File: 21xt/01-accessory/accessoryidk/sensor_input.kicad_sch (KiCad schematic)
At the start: 22 parts, among them IC5 INA821IDGKT, IC6 TXB0108PWR, IC8 INA821IDGKT, IC9 INA821IDGKT, J2 5747847-6, J3 Conn_01x11, J4 Conn_01x11, J5 Conn_01x11

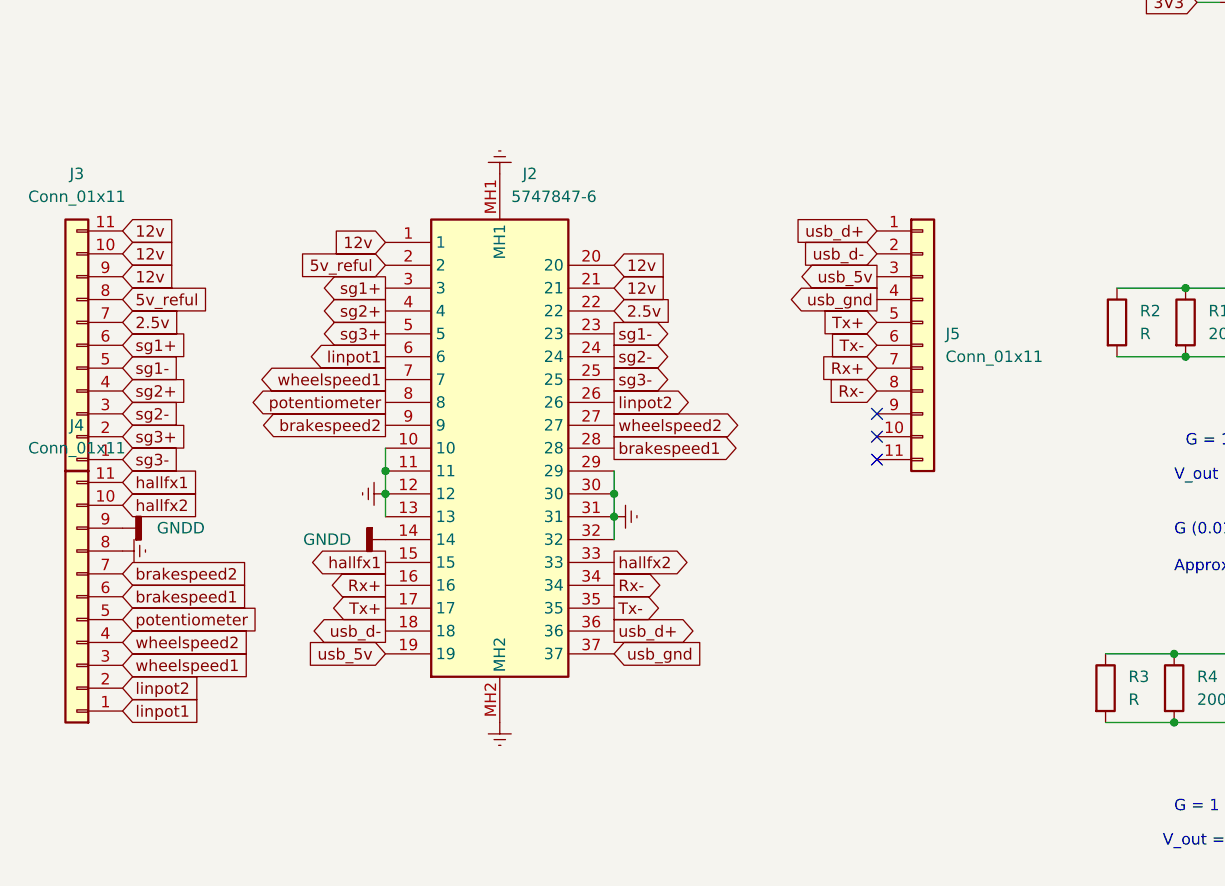
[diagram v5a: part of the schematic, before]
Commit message: Revising accessory schematic
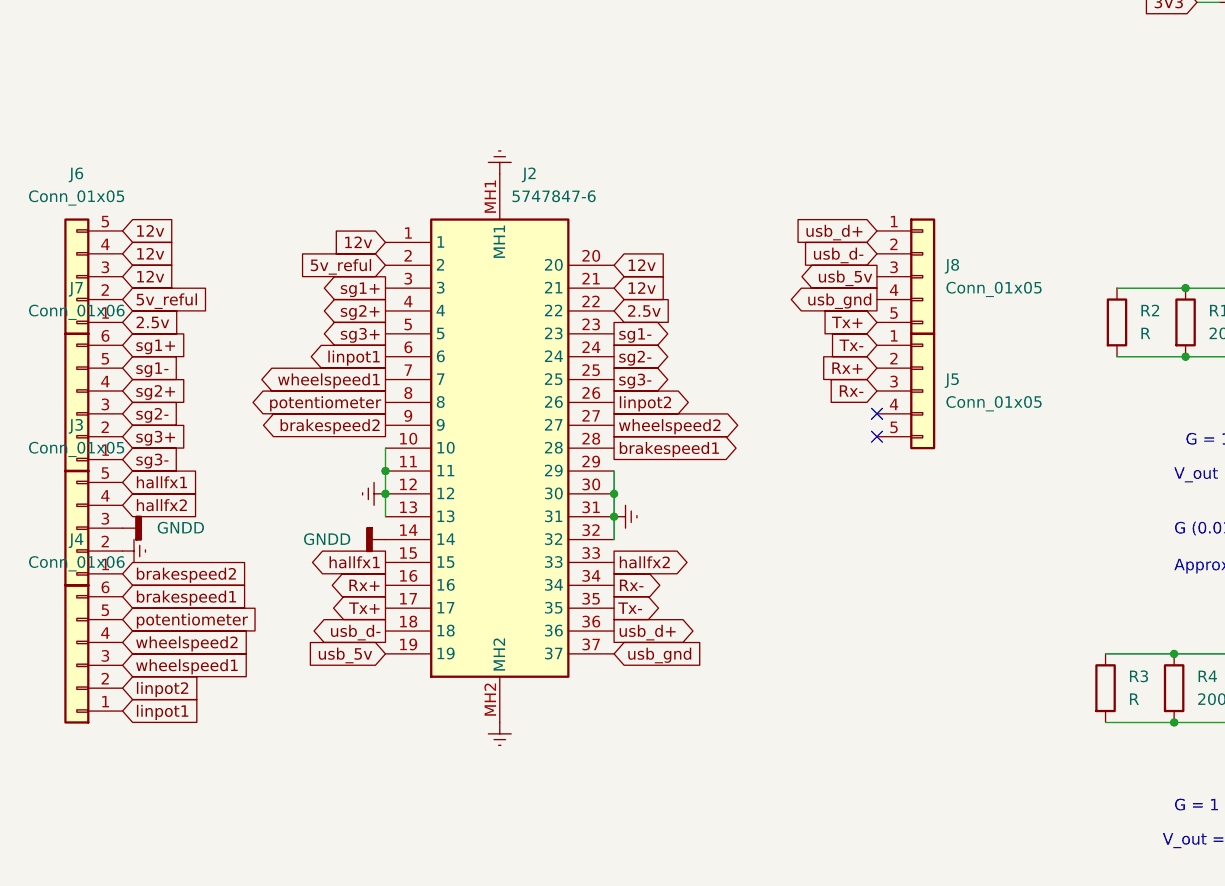
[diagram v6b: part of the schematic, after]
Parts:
- removed J3, J4, J5: Conn_01x11, Connector_JST:JST_EH_B11B-EH-A_1x11_P2.50mm_Vertical, symbol Connector_Generic:Conn_01x11
- added J3, J5, J6, J8: Conn_01x05, symbol Connector_Generic:Conn_01x05
- added J4, J7: Conn_01x06, symbol Connector_Generic:Conn_01x06
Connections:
- net 12v: now also J6.3 (Pin_3), J6.4 (Pin_4), J6.5 (Pin_5)
- net 2.5v: now also J6.1 (Pin_1)
- net 5v_buck: now also J8.3 (Pin_3)
- net 5v_reful: now also J6.2 (Pin_2)
- net Earth: now also J3.2 (Pin_2)
- net GND: now also J8.4 (Pin_4)
- net GNDD: now also J3.3 (Pin_3)
- net Rx+: now also J5.2 (Pin_2)
- net Rx-: now also J5.3 (Pin_3)
- net Tx+: now also J8.5 (Pin_5)
- net Tx-: now also J5.1 (Pin_1)
- net brakespeed1: now also J4.6 (Pin_6)
- net brakespeed2: now also J3.1 (Pin_1)
- net hallfx1: now also J3.5 (Pin_5)
- net hallfx2: now also J3.4 (Pin_4)
- net linpot1: now also J4.1 (Pin_1)
- net linpot2: now also J4.2 (Pin_2)
- net potentiometer: now also J4.5 (Pin_5)
- net sg1+: now also J7.6 (Pin_6)
- net sg1-: now also J7.5 (Pin_5)
- net sg2+: now also J7.4 (Pin_4)
- net sg2-: now also J7.3 (Pin_3)
- net sg3+: now also J7.2 (Pin_2)
- net sg3-: now also J7.1 (Pin_1)
- net usb_d+: now also J8.1 (Pin_1)
- net usb_d-: now also J8.2 (Pin_2)
- net wheelspeed1: now also J4.3 (Pin_3)
- net wheelspeed2: now also J4.4 (Pin_4)
- no-connect marks 15 -> 14
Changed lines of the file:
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@@
   )
   (no_connect (at 143.51 43.18))
-  (no_connect (at 105.41 101.6))
   (no_connect (at 171.45 35.56))
   (no_connect (at 171.45 45.72))
@@
     )
   )
-  (symbol (lib_id "Connector_Generic:Conn_01x11") (at 110.49 88.9 0) (unit 1)
-    (in_bom yes) (on_board yes) (dnp no) (fields_autoplaced)
-    (property "Reference" "J5" (at 113.03 87.63 0)
-      (effects (font (size 1.27 1.27)) (justify left))
-    )
-    (property "Value" "Conn_01x11" (at 113.03 90.17 0)
-      (effects (font (size 1.27 1.27)) (justify left))
-    )
-    (property "Footprint" "Connector_JST:JST_EH_B11B-EH-A_1x11_P2.50mm_Vertical" (at 110.49 88.9 0)
-      (effects (font (size 1.27 1.27)) hide)
-    )
-    (property "Datasheet" "~" (at 110.49 88.9 0)
-      (effects (font (size 1.27 1.27)) hide)
-    )
-    (pin "9")
-    (pin "2")
-    (pin "3")
-    (pin "4")
-    (pin "11")
-    (pin "1")
-    (pin "10")
-    (pin "5")
-    (pin "8")
-    (pin "7")
-    (pin "6")
-    (instances
-      (project "accessoryidk"
-        (path "/5dacc41e-ffff-47d3-9300-200c6018c603/67100f97-5262-4274-9380-0583de02d6bc"
-          (reference "J5") (unit 1)
-        )
-      )
-    )
-  )
   (symbol (lib_id "power:GND") (at 191.77 81.28 90) (unit 1)
     (in_bom yes) (on_board yes) (dnp no) (fields_autoplaced)
@@
         (path "/5dacc41e-ffff-47d3-9300-200c6018c603/67100f97-5262-4274-9380-0583de02d6bc"
           (reference "#PWR022") (unit 1)
-        )
-      )
-    )
-  )
-  (symbol (lib_id "Connector_Generic:Conn_01x11") (at 16.51 116.84 180) (unit 1)
-    (in_bom yes) (on_board yes) (dnp no) (fields_autoplaced)
-    (property "Reference" "J4" (at 16.51 97.79 0)
-      (effects (font (size 1.27 1.27)))
-    )
-    (property "Value" "Conn_01x11" (at 16.51 100.33 0)
-      (effects (font (size 1.27 1.27)))
-    )
-    (property "Footprint" "Connector_JST:JST_EH_B11B-EH-A_1x11_P2.50mm_Vertical" (at 16.51 116.84 0)
-      (effects (font (size 1.27 1.27)) hide)
-    )
-    (property "Datasheet" "~" (at 16.51 116.84 0)
-      (effects (font (size 1.27 1.27)) hide)
-    )
-    (pin "9")
-    (pin "2")
-    (pin "3")
-    (pin "4")
-    (pin "11")
-    (pin "1")
-    (pin "10")
-    (pin "5")
-    (pin "8")
-    (pin "7")
-    (pin "6")
-    (instances
-      (project "accessoryidk"
-        (path "/5dacc41e-ffff-47d3-9300-200c6018c603/67100f97-5262-4274-9380-0583de02d6bc"
-          (reference "J4") (unit 1)
-        )
-      )
-    )
-  )
-  (symbol (lib_id "Connector_Generic:Conn_01x11") (at 16.51 88.9 180) (unit 1)
-    (in_bom yes) (on_board yes) (dnp no) (fields_autoplaced)
-    (property "Reference" "J3" (at 16.51 69.85 0)
-      (effects (font (size 1.27 1.27)))
-    )
-    (property "Value" "Conn_01x11" (at 16.51 72.39 0)
-      (effects (font (size 1.27 1.27)))
-    )
-    (property "Footprint" "Connector_JST:JST_EH_B11B-EH-A_1x11_P2.50mm_Vertical" (at 16.51 88.9 0)
-      (effects (font (size 1.27 1.27)) hide)
-    )
-    (property "Datasheet" "~" (at 16.51 88.9 0)
-      (effects (font (size 1.27 1.27)) hide)
-    )
-    (pin "9")
-    (pin "2")
-    (pin "3")
-    (pin "4")
-    (pin "11")
-    (pin "1")
-    (pin "10")
-    (pin "5")
-    (pin "8")
-    (pin "7")
-    (pin "6")
-    (instances
-      (project "accessoryidk"
-        (path "/5dacc41e-ffff-47d3-9300-200c6018c603/67100f97-5262-4274-9380-0583de02d6bc"
-          (reference "J3") (unit 1)
         )
       )
@@
     )
   )
+  (symbol (lib_id "Connector_Generic:Conn_01x05") (at 16.51 109.22 180) (unit 1)
+    (in_bom yes) (on_board yes) (dnp no) (fields_autoplaced)
+    (property "Reference" "J3" (at 16.51 97.79 0)
+      (effects (font (size 1.27 1.27)))
+    )
+    (property "Value" "Conn_01x05" (at 16.51 100.33 0)
+      (effects (font (size 1.27 1.27)))
+    )
+    (property "Footprint" "" (at 16.51 109.22 0)
+      (effects (font (size 1.27 1.27)) hide)
+    )
+    (property "Datasheet" "~" (at 16.51 109.22 0)
+      (effects (font (size 1.27 1.27)) hide)
+    )
+    (pin "5")
+    (pin "4")
+    (pin "3")
+    (pin "2")
+    (pin "1")
+    (instances
+      (project "accessoryidk"
+        (path "/5dacc41e-ffff-47d3-9300-200c6018c603/67100f97-5262-4274-9380-0583de02d6bc"
+          (reference "J3") (unit 1)
+        )
+      )
+    )
+  )
   (symbol (lib_id "power:GND") (at 267.97 121.92 90) (unit 1)
     (in_bom yes) (on_board yes) (dnp no) (fields_autoplaced)
@@
         (path "/5dacc41e-ffff-47d3-9300-200c6018c603/67100f97-5262-4274-9380-0583de02d6bc"
           (reference "R4") (unit 1)
+        )
+      )
+    )
+  )
+  (symbol (lib_id "Connector_Generic:Conn_01x05") (at 110.49 81.28 0) (unit 1)
+    (in_bom yes) (on_board yes) (dnp no) (fields_autoplaced)
+    (property "Reference" "J8" (at 113.03 80.01 0)
+      (effects (font (size 1.27 1.27)) (justify left))
+    )
+    (property "Value" "Conn_01x05" (at 113.03 82.55 0)
+      (effects (font (size 1.27 1.27)) (justify left))
+    )
+    (property "Footprint" "" (at 110.49 81.28 0)
+      (effects (font (size 1.27 1.27)) hide)
+    )
+    (property "Datasheet" "~" (at 110.49 81.28 0)
+      (effects (font (size 1.27 1.27)) hide)
+    )
+    (pin "5")
+    (pin "4")
+    (pin "3")
+    (pin "2")
+    (pin "1")
+    (instances
+      (project "accessoryidk"
+        (path "/5dacc41e-ffff-47d3-9300-200c6018c603/67100f97-5262-4274-9380-0583de02d6bc"
+          (reference "J8") (unit 1)
+        )
+      )
+    )
+  )
+  (symbol (lib_id "Connector_Generic:Conn_01x05") (at 110.49 93.98 0) (unit 1)
+    (in_bom yes) (on_board yes) (dnp no) (fields_autoplaced)
+    (property "Reference" "J5" (at 113.03 92.71 0)
+      (effects (font (size 1.27 1.27)) (justify left))
+    )
+    (property "Value" "Conn_01x05" (at 113.03 95.25 0)
+      (effects (font (size 1.27 1.27)) (justify left))
+    )
+    (property "Footprint" "" (at 110.49 93.98 0)
+      (effects (font (size 1.27 1.27)) hide)
+    )
+    (property "Datasheet" "~" (at 110.49 93.98 0)
+      (effects (font (size 1.27 1.27)) hide)
+    )
+    (pin "5")
+    (pin "4")
+    (pin "3")
+    (pin "2")
+    (pin "1")
+    (instances
+      (project "accessoryidk"
+        (path "/5dacc41e-ffff-47d3-9300-200c6018c603/67100f97-5262-4274-9380-0583de02d6bc"
+          (reference "J5") (unit 1)
         )
       )
@@
         (path "/5dacc41e-ffff-47d3-9300-200c6018c603/67100f97-5262-4274-9380-0583de02d6bc"
           (reference "#PWR050") (unit 1)
+        )
+      )
+    )
+  )
+  (symbol (lib_id "Connector_Generic:Conn_01x06") (at 16.51 96.52 180) (unit 1)
+    (in_bom yes) (on_board yes) (dnp no) (fields_autoplaced)
+    (property "Reference" "J7" (at 16.51 82.55 0)
+      (effects (font (size 1.27 1.27)))
+    )
+    (property "Value" "Conn_01x06" (at 16.51 85.09 0)
+      (effects (font (size 1.27 1.27)))
+    )
+    (property "Footprint" "" (at 16.51 96.52 0)
+      (effects (font (size 1.27 1.27)) hide)
+    )
+    (property "Datasheet" "~" (at 16.51 96.52 0)
+      (effects (font (size 1.27 1.27)) hide)
+    )
+    (pin "6")
+    (pin "5")
+    (pin "3")
+    (pin "2")
+    (pin "1")
+    (pin "4")
+    (instances
+      (project "accessoryidk"
+        (path "/5dacc41e-ffff-47d3-9300-200c6018c603/67100f97-5262-4274-9380-0583de02d6bc"
+          (reference "J7") (unit 1)
         )
       )
@@
     )
   )
+  (symbol (lib_id "Connector_Generic:Conn_01x05") (at 16.51 81.28 180) (unit 1)
+    (in_bom yes) (on_board yes) (dnp no) (fields_autoplaced)
+    (property "Reference" "J6" (at 16.51 69.85 0)
+      (effects (font (size 1.27 1.27)))
+    )
+    (property "Value" "Conn_01x05" (at 16.51 72.39 0)
+      (effects (font (size 1.27 1.27)))
+    )
+    (property "Footprint" "" (at 16.51 81.28 0)
+      (effects (font (size 1.27 1.27)) hide)
+    )
+    (property "Datasheet" "~" (at 16.51 81.28 0)
+      (effects (font (size 1.27 1.27)) hide)
+    )
+    (pin "5")
+    (pin "4")
+    (pin "3")
+    (pin "2")
+    (pin "1")
+    (instances
+      (project "accessoryidk"
+        (path "/5dacc41e-ffff-47d3-9300-200c6018c603/67100f97-5262-4274-9380-0583de02d6bc"
+          (reference "J6") (unit 1)
+        )
+      )
+    )
+  )
   (symbol (lib_id "power:GND") (at 260.35 137.16 0) (unit 1)
     (in_bom yes) (on_board yes) (dnp no) (fields_autoplaced)
@@
         )
       )
+    )
+  )
+  (symbol (lib_id "Connector_Generic:Conn_01x06") (at 16.51 124.46 180) (unit 1)
+    (in_bom yes) (on_board yes) (dnp no) (fields_autoplaced)
+    (property "Reference" "J4" (at 16.51 110.49 0)
+      (effects (font (size 1.27 1.27)))
+    )
+    (property "Value" "Conn_01x06" (at 16.51 113.03 0)
+      (effects (font (size 1.27 1.27)))
+    )
+    (property "Footprint" "" (at 16.51 124.46 0)
+      (effects (font (size 1.27 1.27)) hide)
+    )
+    (property "Datasheet" "~" (at 16.51 124.46 0)
+      (effects (font (size 1.27 1.27)) hide)
+    )
+    (pin "6")
+    (pin "5")
+    (pin "3")
+    (pin "2")
+    (pin "1")
+    (pin "4")
+    (instances
+      (project "accessoryidk"
+        (path "/5dacc41e-ffff-47d3-9300-200c6018c603/67100f97-5262-4274-9380-0583de02d6bc"
+          (reference "J4") (unit 1)
+        )
+      )
